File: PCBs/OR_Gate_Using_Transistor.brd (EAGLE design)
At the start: 30 x 37 mm, 11 parts, among them T1 2N3904, T2 2N3904

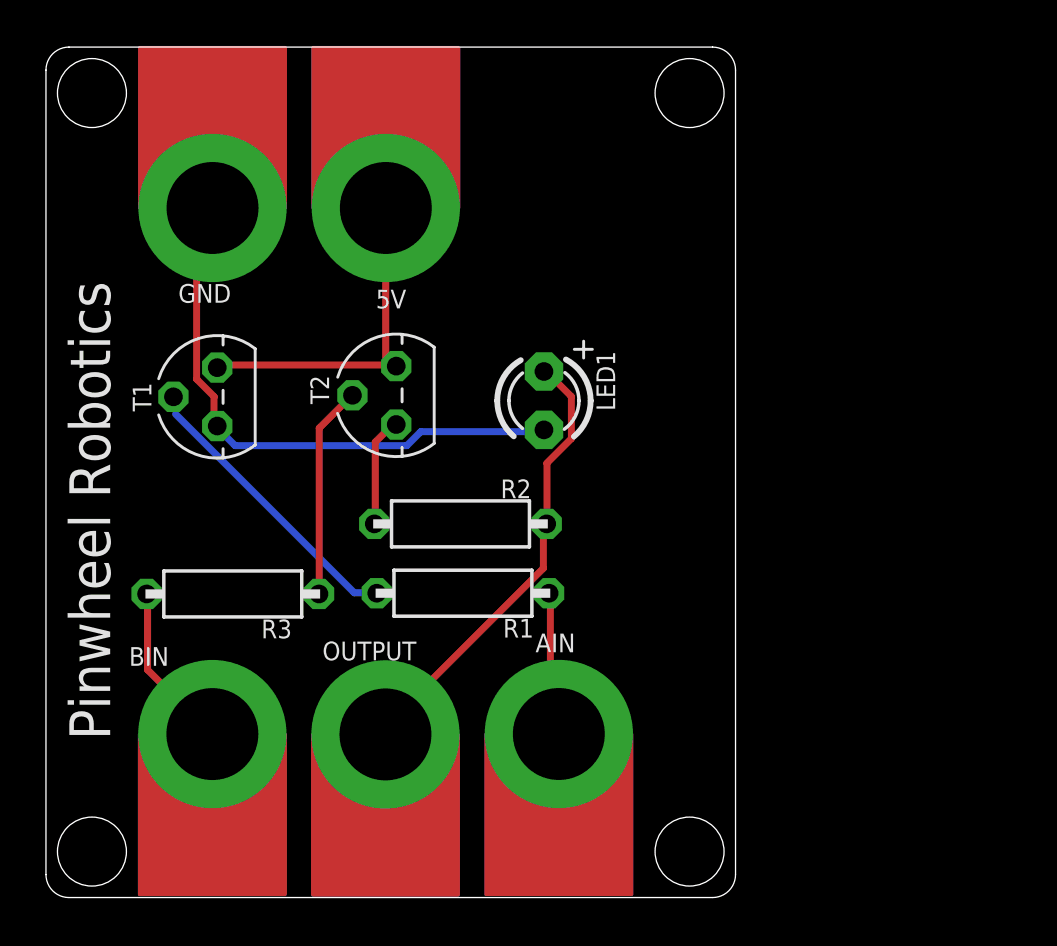
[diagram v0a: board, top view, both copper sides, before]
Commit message: Update for Dim width is 42 length is 28 for type 2 pcb
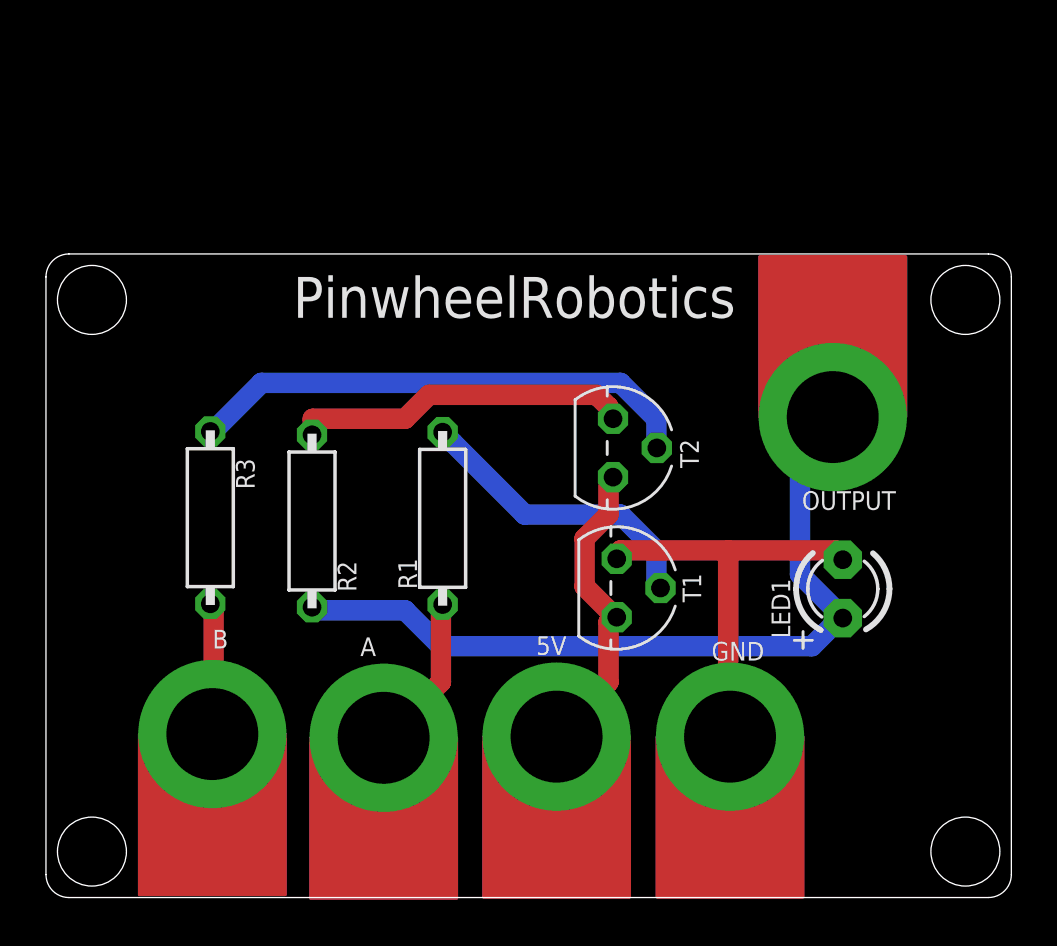
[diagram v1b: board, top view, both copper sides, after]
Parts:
- removed AIN: MICROBIT_PAD, microbit:MICROBIT_PAD
- added A: MICROBIT_PAD, microbit:MICROBIT_PAD
- moved GND 32.2 mm to (29.8, 7.00), turned to 0 degrees
- moved 5V 24.2 mm to (22.2, 7.00), turned to 0 degrees
- moved OUTPUT 23.9 mm to (34.2, 20.9), turned to 180 degrees
- moved T1 19.3 mm to (24.8, 13.5), turned to 270 degrees
- moved LED1 15.4 mm to (34.7, 13.4), turned to 90 degrees
- moved T2 9.71 mm to (24.7, 19.6), turned to 270 degrees
- moved R2 6.46 mm to (11.6, 16.4), turned to 90 degrees
- moved R3 3.46 mm to (7.15, 16.5), turned to 270 degrees
- moved R1 3.37 mm to (17.3, 16.5), turned to 90 degrees
- renumbered BIN to B
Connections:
- net N$5: now also A.PAD; no longer AIN.PAD
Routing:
- net N$6: track 19.7 -> 34.6 mm
- net N$3: track 9.25 -> 22.2 mm
- net N$7: track 4.80 -> 14.8 mm
- net GND: track 25.0 -> 18.4 mm
- net 5V: track 15.2 -> 13.6 mm
- net N$2: track 7.28 -> 5.71 mm
- net N$5: track 6.29 -> 6.86 mm
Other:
- board size 30 x 37 mm -> 42 x 28 mm
- board text added: "PinwheelRobotics"
- board text removed: "Pinwheel Robotics"
